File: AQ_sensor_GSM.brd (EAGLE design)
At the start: 110 x 64 mm, 49 parts, among them IC2 MCP73831/OT, J1 F-1X03-SIP-100-32, SW1 PCM12SMTR, SW2 PCM12SMTR, U2 TEXAS_INSTRUMENTS_SN74HC125TE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, U3 TEXAS_INSTRUMENTS_LM1117IMP-3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, X1 53048-08, X2 SIMLOCK-C707_10M006_512_2, X4 50 Ohms

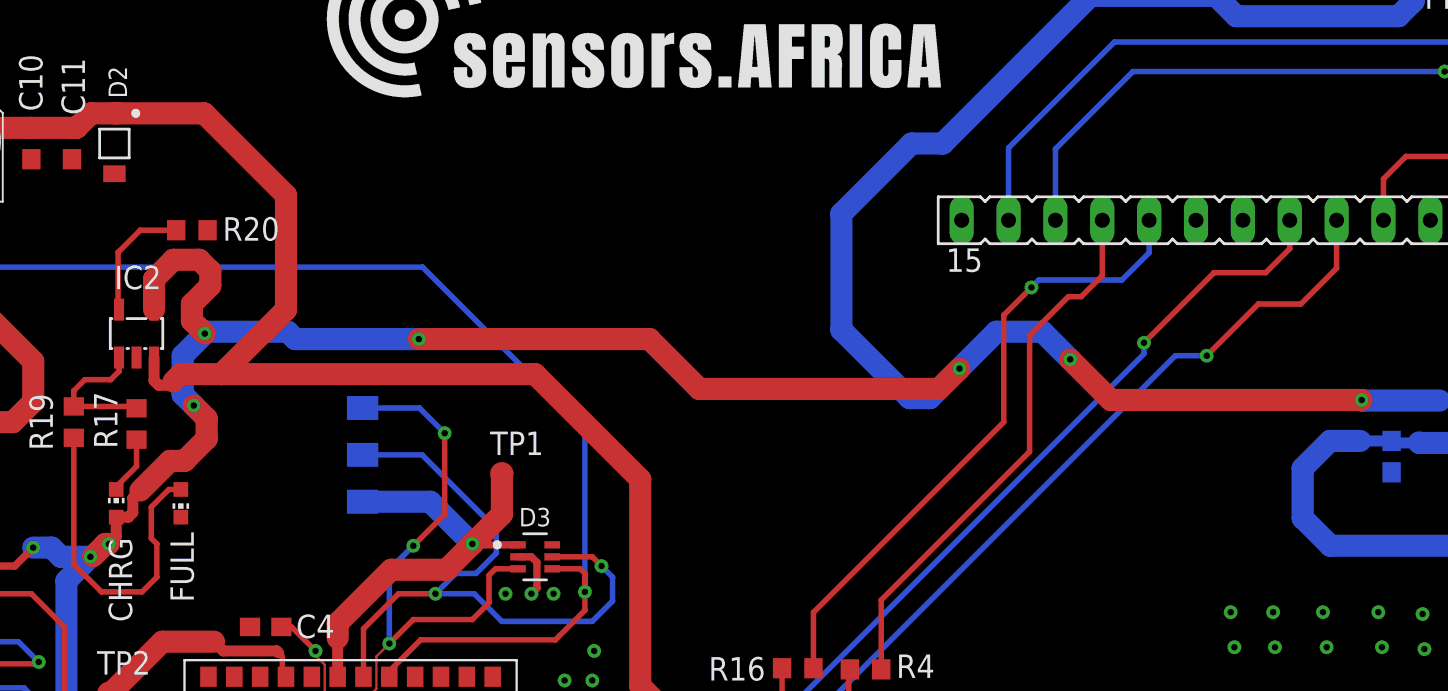
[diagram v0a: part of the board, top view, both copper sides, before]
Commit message: Added copper fills
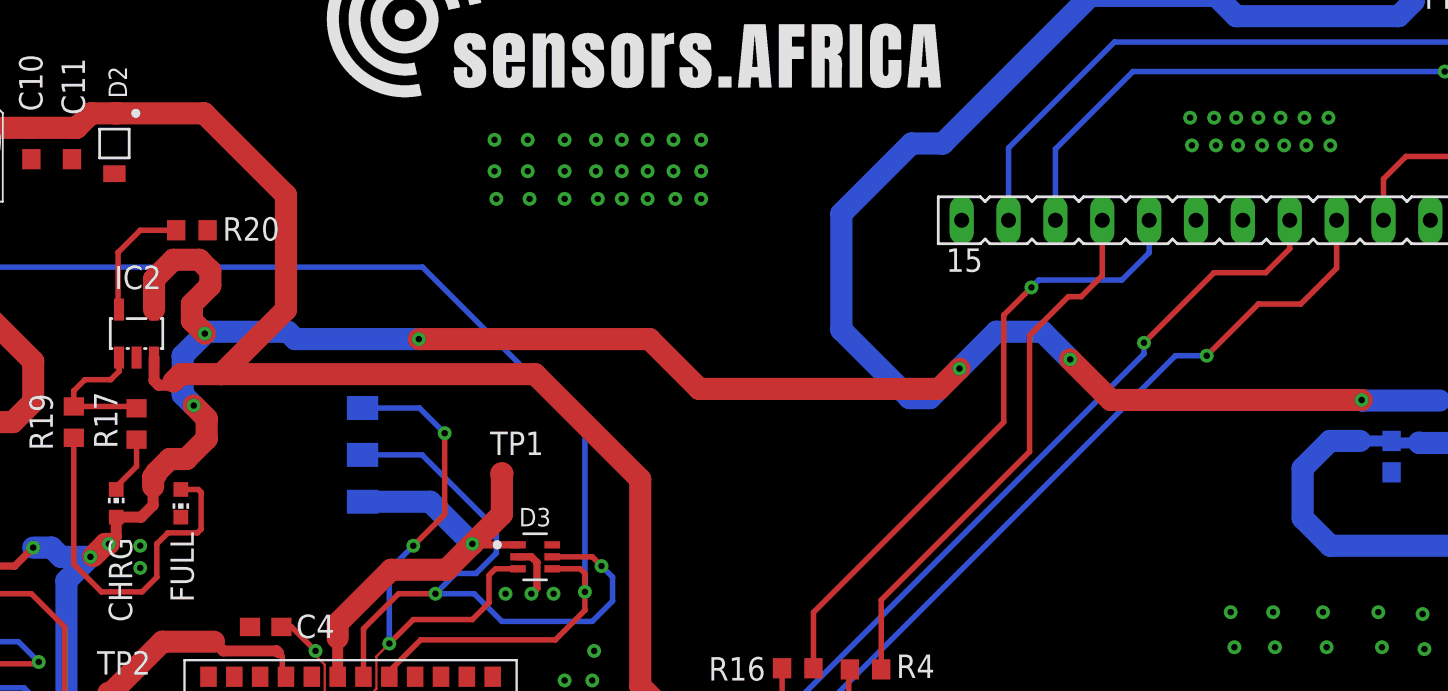
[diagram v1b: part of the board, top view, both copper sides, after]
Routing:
- net N$12: track 18.2 -> 20.0 mm
- net +5V: track 276.6 -> 277.6 mm
- net GND: vias 59 -> 99
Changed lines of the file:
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@@
 <text x="79.6" y="1.3" size="1.778" layer="25">ON</text>
 <text x="92.5" y="1.3" size="1.778" layer="25">OFF</text>
+<dimension x1="0" y1="64" x2="110" y2="64" x3="55" y3="70.2" textsize="1.778" layer="25" dtype="horizontal"/>
+<dimension x1="110" y1="64" x2="110" y2="0" x3="117.8" y3="32" textsize="1.778" layer="25" dtype="vertical"/>
 </plain>
 <attributes>
@@
 <via x="63.1" y="7.3" extent="1-16" drill="0.35"/>
 <via x="64.6" y="7.3" extent="1-16" drill="0.35"/>
+<via x="36.9" y="49.3" extent="1-16" drill="0.35"/>
+<via x="38.7" y="49.3" extent="1-16" drill="0.35"/>
+<via x="40.7" y="49.3" extent="1-16" drill="0.35"/>
+<via x="42.4" y="49.3" extent="1-16" drill="0.35"/>
+<via x="43.8" y="49.3" extent="1-16" drill="0.35"/>
+<via x="45.2" y="49.3" extent="1-16" drill="0.35"/>
+<via x="46.6" y="49.3" extent="1-16" drill="0.35"/>
+<via x="48.1" y="49.3" extent="1-16" drill="0.35"/>
+<via x="36.9" y="47.6" extent="1-16" drill="0.35"/>
+<via x="38.7" y="47.6" extent="1-16" drill="0.35"/>
+<via x="40.7" y="47.6" extent="1-16" drill="0.35"/>
+<via x="42.4" y="47.6" extent="1-16" drill="0.35"/>
+<via x="43.8" y="47.6" extent="1-16" drill="0.35"/>
+<via x="45.2" y="47.6" extent="1-16" drill="0.35"/>
+<via x="46.6" y="47.6" extent="1-16" drill="0.35"/>
+<via x="48.1" y="47.6" extent="1-16" drill="0.35"/>
+<via x="37" y="46.1" extent="1-16" drill="0.35"/>
+<via x="38.8" y="46.1" extent="1-16" drill="0.35"/>
+<via x="40.7" y="46.1" extent="1-16" drill="0.35"/>
+<via x="42.5" y="46.1" extent="1-16" drill="0.35"/>
+<via x="43.8" y="46.1" extent="1-16" drill="0.35"/>
+<via x="45.2" y="46.1" extent="1-16" drill="0.35"/>
+<via x="46.7" y="46.1" extent="1-16" drill="0.35"/>
+<via x="48.1" y="46.1" extent="1-16" drill="0.35"/>
+<via x="17.7" y="27.3" extent="1-16" drill="0.35"/>
+<via x="17.7" y="26.1" extent="1-16" drill="0.35"/>
+<via x="74.6" y="50.5" extent="1-16" drill="0.35"/>
+<via x="75.9" y="50.5" extent="1-16" drill="0.35"/>
+<via x="77.1" y="50.5" extent="1-16" drill="0.35"/>
+<via x="78.3" y="50.5" extent="1-16" drill="0.35"/>
+<via x="79.5" y="50.5" extent="1-16" drill="0.35"/>
+<via x="80.8" y="50.5" extent="1-16" drill="0.35"/>
+<via x="82.1" y="50.5" extent="1-16" drill="0.35"/>
+<via x="74.7" y="49" extent="1-16" drill="0.35"/>
+<via x="76" y="49" extent="1-16" drill="0.35"/>
+<via x="77.2" y="49" extent="1-16" drill="0.35"/>
+<via x="78.5" y="49" extent="1-16" drill="0.35"/>
+<via x="79.7" y="49" extent="1-16" drill="0.35"/>
+<via x="80.9" y="49" extent="1-16" drill="0.35"/>
+<via x="82.2" y="49" extent="1-16" drill="0.35"/>
 <wire x1="15.825" y1="8.84" x2="15.825" y2="5.03" width="0" layer="19" extent="1-1"/>
 </signal>
@@
 <wire x1="20.6" y1="34.9" x2="21.3" y2="34.2" width="1.2" layer="1"/>
 <wire x1="21.3" y1="34.2" x2="21.3" y2="33.1" width="1.2" layer="1"/>
-<wire x1="21.3" y1="33.1" x2="20.1" y2="31.9" width="1.2" layer="1"/>
-<wire x1="20.1" y1="31.9" x2="19.315075" y2="31.9" width="1.2" layer="1"/>
-<wire x1="19.315075" y1="31.9" x2="17.7075375" y2="30.2924625" width="1.2" layer="1"/>
-<wire x1="17.7075375" y1="30.2924625" x2="17.3" y2="29.884925" width="0.6" layer="1"/>
-<wire x1="17.05" y1="28.85" x2="16.4" y2="28.85" width="0.6" layer="1"/>
-<wire x1="17.3" y1="29.884925" x2="17.3" y2="29.1" width="0.6" layer="1"/>
-<wire x1="17.3" y1="29.1" x2="17.05" y2="28.85" width="0.6" layer="1"/>
 <wire x1="62.1" y1="36.9" x2="60.5" y2="35.3" width="1.2" layer="16"/>
 <wire x1="60.5" y1="35.3" x2="59.4" y2="35.3" width="1.2" layer="16"/>
@@
 <wire x1="18.45" y1="41.75" x2="19.5" y2="42.8" width="1.2" layer="1"/>
 <wire x1="19.5" y1="42.8" x2="20.9" y2="42.8" width="1.2" layer="1"/>
+<wire x1="21.3" y1="33.1" x2="20.2" y2="32" width="1.2" layer="1"/>
+<wire x1="18.55" y1="31.25" x2="18.55" y2="31.165075" width="1.2" layer="1"/>
+<wire x1="18.55" y1="31.165075" x2="18.4" y2="31.015075" width="1.2" layer="1"/>
+<wire x1="18.4" y1="31.015075" x2="18.4" y2="30.5" width="1.2" layer="1"/>
+<wire x1="20.2" y1="32" x2="19.3" y2="32" width="1.2" layer="1"/>
+<wire x1="19.3" y1="32" x2="18.55" y2="31.25" width="1.2" layer="1"/>
+<wire x1="18.4" y1="29.5" x2="18.4" y2="31.015075" width="0.6" layer="1"/>
+<wire x1="16.4" y1="28.85" x2="17.75" y2="28.85" width="0.6" layer="1"/>
+<wire x1="17.75" y1="28.85" x2="18.4" y2="29.5" width="0.6" layer="1"/>
 <wire x1="15" y1="26.7" x2="15.15" y2="26.734925" width="0" layer="19" extent="1-1"/>
 </signal>
@@
 <contactref element="FULL" pad="A"/>
 <contactref element="R19" pad="1"/>
-<wire x1="18.3" y1="27.7" x2="18.3" y2="29.4" width="0.3" layer="1"/>
-<wire x1="18.3" y1="29.4" x2="19.25" y2="30.35" width="0.3" layer="1"/>
-<wire x1="19.25" y1="30.35" x2="19.9" y2="30.35" width="0.3" layer="1"/>
 <wire x1="15.6" y1="24.8" x2="17.8" y2="24.8" width="0.3" layer="1"/>
 <wire x1="17.8" y1="24.8" x2="18.6" y2="25.6" width="0.3" layer="1"/>
-<wire x1="18.6" y1="27.4" x2="18.3" y2="27.7" width="0.3" layer="1"/>
 <wire x1="14.1" y1="33.15" x2="14.1" y2="26.3" width="0.3" layer="1"/>
 <wire x1="14.1" y1="26.3" x2="15.6" y2="24.8" width="0.3" layer="1"/>
-<wire x1="18.6" y1="25.6" x2="18.6" y2="27.4" width="0.3" layer="1"/>
+<wire x1="18.6" y1="27.4" x2="18.6" y2="25.6" width="0.3" layer="1"/>
+<wire x1="19.9" y1="30.35" x2="20.85" y2="30.35" width="0.3" layer="1"/>
+<wire x1="20.85" y1="30.35" x2="21" y2="30.2" width="0.3" layer="1"/>
+<wire x1="19.2" y1="28" x2="18.6" y2="27.4" width="0.3" layer="1"/>
+<wire x1="21" y1="30.2" x2="21" y2="28.2" width="0.3" layer="1"/>
+<wire x1="21" y1="28.2" x2="20.8" y2="28" width="0.3" layer="1"/>
+<wire x1="20.8" y1="28" x2="19.2" y2="28" width="0.3" layer="1"/>
 </signal>
 <signal name="N$13">

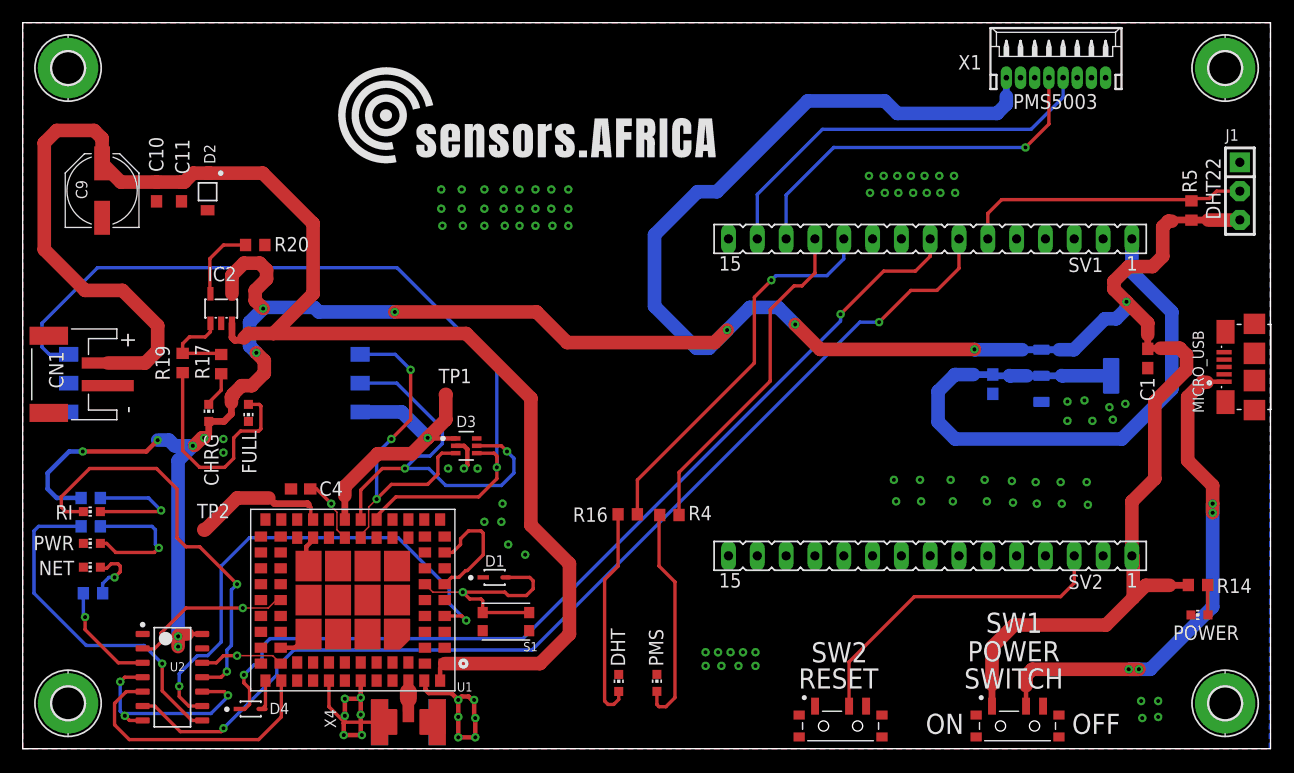
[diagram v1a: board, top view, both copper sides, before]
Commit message: Added stitching vias
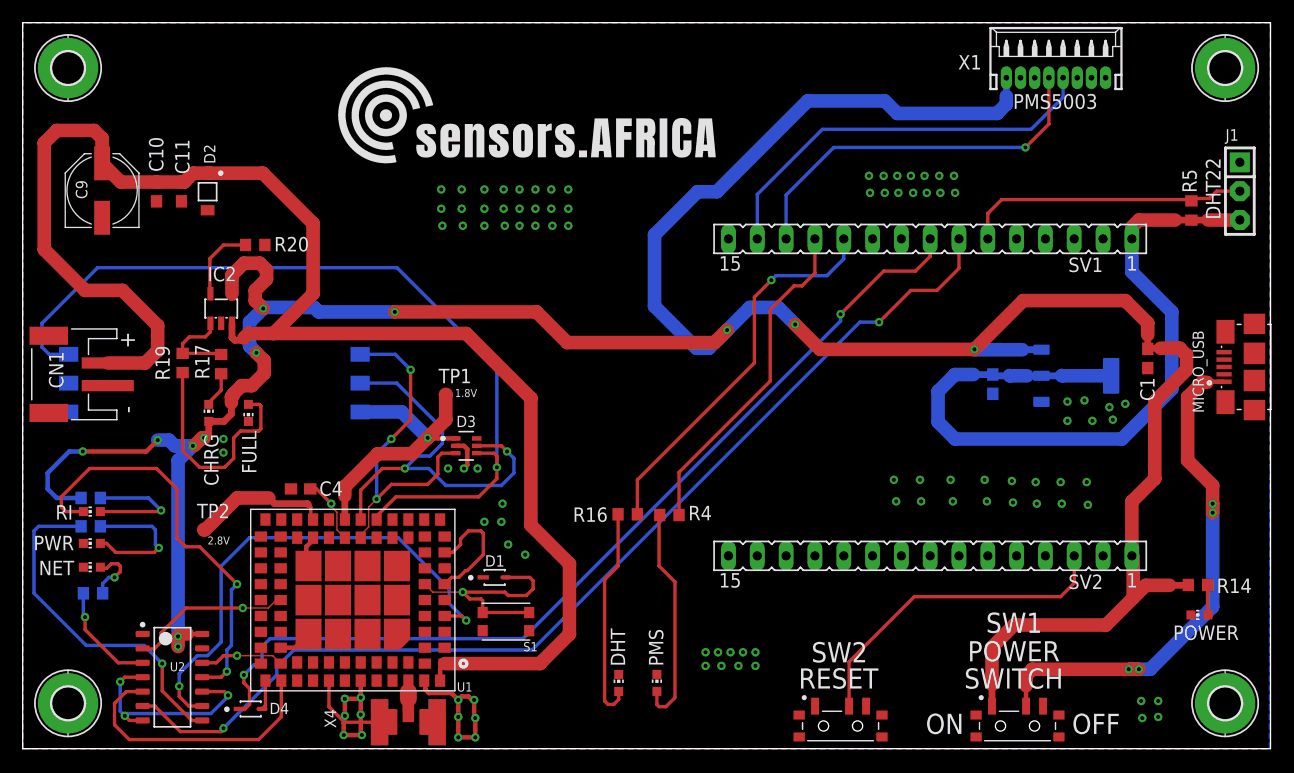
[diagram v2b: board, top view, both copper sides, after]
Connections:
- net +3V3: now also J1.3, R5.1
- net +5V: no longer J1.3, R5.1
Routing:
- net +5V: track 277.6 -> 265.7 mm, vias 13 -> 12
- net +3V3: track 56.9 -> 67.8 mm
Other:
- board text added: "1.8V"
- board text added: "2.8V"
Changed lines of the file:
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@@
 <drawing>
 <settings>
-<setting alwaysvectorfont="yes"/>
+<setting alwaysvectorfont="no"/>
 <setting verticaltext="up"/>
 </settings>
@@
 <dimension x1="0" y1="64" x2="110" y2="64" x3="55" y3="70.2" textsize="1.778" layer="25" dtype="horizontal"/>
 <dimension x1="110" y1="64" x2="110" y2="0" x3="117.8" y3="32" textsize="1.778" layer="25" dtype="vertical"/>
+<text x="38.1" y="31" size="0.7" layer="25">1.8V</text>
+<text x="16.3" y="18" size="0.7" layer="25">2.8V</text>
 </plain>
 <attributes>
@@
 <contactref element="C1" pad="1"/>
 <contactref element="U3" pad="3"/>
-<contactref element="J1" pad="3"/>
-<contactref element="R5" pad="1"/>
 <contactref element="SW1" pad="1"/>
 <contactref element="IC2" pad="4"/>
@@
 <wire x1="3" y1="22.1" x2="5.15" y2="22.1" width="0.4" layer="16"/>
 <wire x1="4.1" y1="26.2" x2="2.2" y2="24.3" width="0.4" layer="16"/>
-<wire x1="103.05" y1="46.61" x2="103.03" y2="46.59" width="0.4" layer="1"/>
 <wire x1="85.45" y1="3.75" x2="85.45" y2="5.65" width="0.6" layer="1"/>
 <wire x1="85.5" y1="5.7" x2="85.45" y2="5.65" width="0.6" layer="1"/>
@@
 <wire x1="99.18" y1="36.48" x2="99.2" y2="36.5" width="0.6" layer="1"/>
 <wire x1="99.18" y1="36.48" x2="99.18" y2="37.52" width="1.2" layer="1"/>
-<wire x1="99.18" y1="37.52" x2="97.3" y2="39.4" width="1.2" layer="1"/>
-<via x="97.3" y="39.4" extent="1-16" drill="0.35"/>
-<wire x1="97.3" y1="39.4" x2="96.2" y2="40.5" width="1.2" layer="1"/>
-<wire x1="97.5" y1="42.5" x2="99.6" y2="42.5" width="1.2" layer="1"/>
-<wire x1="99.6" y1="42.5" x2="100.5" y2="43.4" width="1.2" layer="1"/>
-<wire x1="96.2" y1="40.5" x2="96.2" y2="41.2" width="1.2" layer="1"/>
-<wire x1="96.2" y1="41.2" x2="97.5" y2="42.5" width="1.2" layer="1"/>
-<wire x1="101.3" y1="46.5" x2="101" y2="46.5" width="1.2" layer="1"/>
-<wire x1="100.5" y1="43.4" x2="100.5" y2="46" width="1.2" layer="1"/>
-<wire x1="100.5" y1="46" x2="101" y2="46.5" width="1.2" layer="1"/>
-<wire x1="101" y1="46.5" x2="101.11" y2="46.61" width="0.6" layer="1"/>
-<wire x1="101.11" y1="46.61" x2="103.05" y2="46.61" width="0.6" layer="1"/>
-<wire x1="103.03" y1="46.59" x2="103.04" y2="46.6" width="0.6" layer="1"/>
-<wire x1="103.04" y1="46.6" x2="104.5" y2="46.6" width="0.6" layer="1"/>
-<wire x1="104.5" y1="46.6" x2="107.29" y2="46.6" width="1.2" layer="1"/>
-<wire x1="107.29" y1="46.6" x2="107.3" y2="46.61" width="1.2" layer="1"/>
-<wire x1="89.805" y1="35.17" x2="91.37" y2="35.17" width="0.6" layer="16"/>
-<wire x1="91.37" y1="35.17" x2="91.4" y2="35.2" width="0.6" layer="16"/>
-<wire x1="91.37" y1="35.17" x2="92.67" y2="35.17" width="1.2" layer="16"/>
-<wire x1="95.4" y1="37.9" x2="96.4" y2="37.9" width="1.2" layer="16"/>
-<wire x1="96.4" y1="37.9" x2="97.3" y2="38.8" width="1.2" layer="16"/>
-<wire x1="97.3" y1="38.8" x2="97.3" y2="39.4" width="1.2" layer="16"/>
-<wire x1="92.67" y1="35.17" x2="95.4" y2="37.9" width="1.2" layer="16"/>
 <wire x1="89.805" y1="35.17" x2="88.13" y2="35.17" width="0.6" layer="16"/>
 <wire x1="88.13" y1="35.17" x2="88.1" y2="35.2" width="0.6" layer="16"/>
@@
 <wire x1="16.4" y1="28.85" x2="17.75" y2="28.85" width="0.6" layer="1"/>
 <wire x1="17.75" y1="28.85" x2="18.4" y2="29.5" width="0.6" layer="1"/>
+<wire x1="99.18" y1="37.52" x2="97.2" y2="39.5" width="1.2" layer="1"/>
+<wire x1="88.2" y1="39.5" x2="83.9" y2="35.2" width="1.2" layer="1"/>
+<wire x1="97.2" y1="39.5" x2="88.2" y2="39.5" width="1.2" layer="1"/>
 <wire x1="15" y1="26.7" x2="15.15" y2="26.734925" width="0" layer="19" extent="1-1"/>
 </signal>
@@
 <wire x1="101.3" y1="31.7" x2="101.3" y2="38.5" width="1.2" layer="16"/>
 <wire x1="101.3" y1="38.5" x2="97.78" y2="42.02" width="1.2" layer="16"/>
+<contactref element="J1" pad="3"/>
+<contactref element="R5" pad="1"/>
+<wire x1="103.03" y1="46.59" x2="103.04" y2="46.6" width="0.6" layer="1"/>
+<wire x1="103.04" y1="46.6" x2="104.5" y2="46.6" width="0.6" layer="1"/>
+<wire x1="104.5" y1="46.6" x2="107.29" y2="46.6" width="1.2" layer="1"/>
+<wire x1="97.78" y1="44.94" x2="97.78" y2="45.98" width="1.2" layer="1"/>
+<wire x1="98.4" y1="46.6" x2="101.6" y2="46.6" width="1.2" layer="1"/>
+<wire x1="97.78" y1="45.98" x2="98.4" y2="46.6" width="1.2" layer="1"/>
+<wire x1="101.6" y1="46.6" x2="103.04" y2="46.6" width="0.6" layer="1"/>
+<wire x1="107.29" y1="46.6" x2="107.3" y2="46.61" width="0" layer="19" extent="1-1"/>
 </signal>
 <signal name="DHT_OUT">
